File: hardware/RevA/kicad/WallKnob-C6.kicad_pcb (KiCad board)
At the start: 2 copper layers, 58 x 58 mm, 10 parts, among them SW1 EC11+PUSH, U1 ESP32-C6-MINI-1

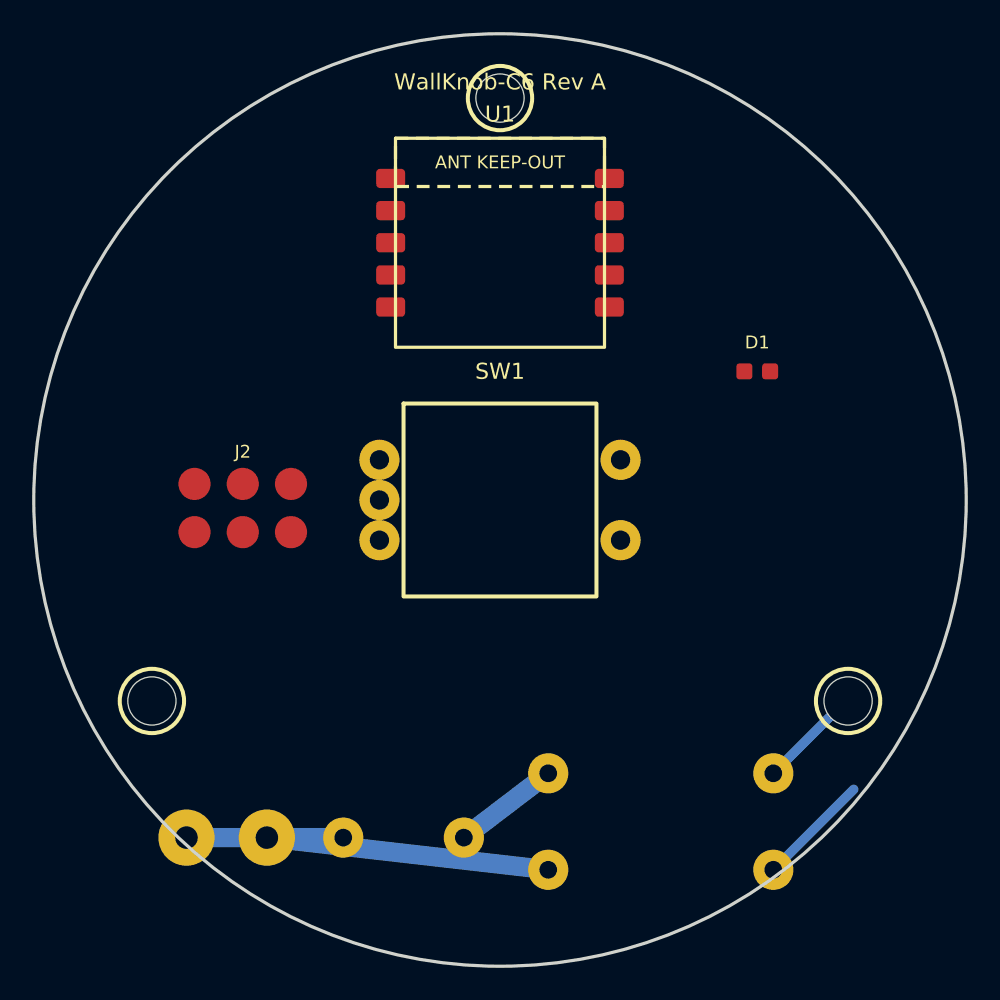
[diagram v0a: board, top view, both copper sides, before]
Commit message: Fix Rev A component placement inside PCB outline
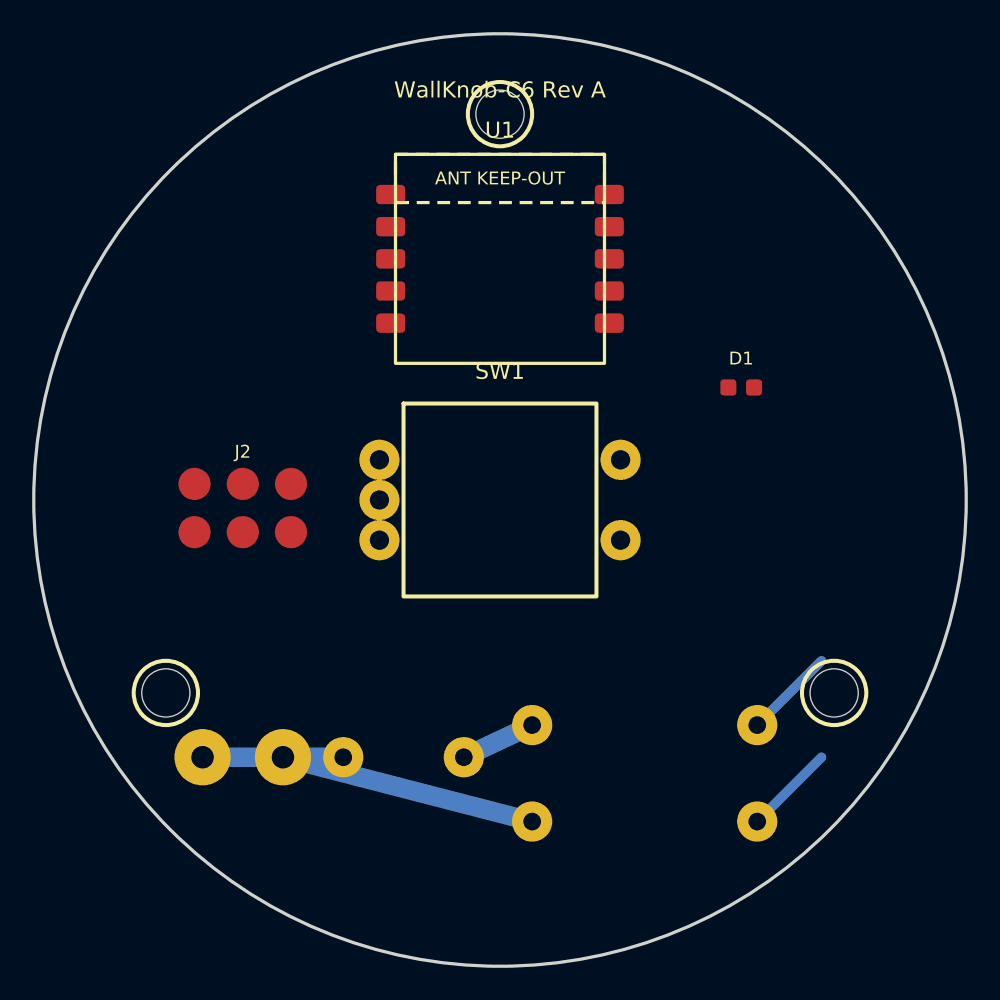
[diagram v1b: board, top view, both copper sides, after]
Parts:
- moved J1 5.10 mm to (84.0, 116.0)
- moved F1 5.00 mm to (94.0, 116.0)
- moved PS1 3.16 mm to (109.0, 117.0)
- moved D1 1.41 mm to (115.0, 93.0)
- moved H2 1.00 mm to (79.2, 112.0)
- moved H3 1.00 mm to (120.8, 112.0)
- moved H1 1.00 mm to (100.0, 76.0)
- moved U1 1.00 mm to (100.0, 85.0)
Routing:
- net L_FUSED: track 6.60 -> 4.70 mm
- net N_IN: track 17.6 -> 16.0 mm
- net GND: track 7.07 -> 5.66 mm
- net L_IN: track 9.75 -> 8.75 mm
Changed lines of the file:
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@@
   (net 13 "UART_RX")
   (gr_circle (center 100 100) (end 129 100) (stroke (width 0.2) (type solid)) (fill none) (layer "Edge.Cuts"))
-  (gr_line (start 82 112) (end 118 112) (stroke (width 0.3) (type solid)) (layer "B.SilkS"))
-  (gr_text "PRIMARY" (at 100 119) (layer "B.SilkS") (effects (font (size 1 1) (thickness 0.18)) (justify mirror)))
+  (gr_line (start 78 111) (end 122 111) (stroke (width 0.3) (type solid)) (layer "B.SilkS"))
+  (gr_text "PRIMARY" (at 100 117) (layer "B.SilkS") (effects (font (size 1 1) (thickness 0.18)) (justify mirror)))
   (gr_text "SELV" (at 100 106) (layer "B.SilkS") (effects (font (size 1 1) (thickness 0.18)) (justify mirror)))
-  (gr_text "WallKnob-C6 Rev A" (at 100 74) (layer "F.SilkS") (effects (font (size 1 1) (thickness 0.18))))
-  (footprint "MountingHole_1" (layer "F.Cu") (at 100.000 75.000)
+  (gr_text "WallKnob-C6 Rev A" (at 100 74.5) (layer "F.SilkS") (effects (font (size 1 1) (thickness 0.18))))
+  (footprint "MountingHole_1" (layer "F.Cu") (at 100.000 76.000)
     (property "Reference" "H1" (at 0 -3 0) (layer "F.SilkS") hide (effects (font (size 1 1) (thickness 0.15))))
     (fp_circle (center 0 0) (end 2 0) (stroke (width 0.25) (type solid)) (fill none) (layer "F.SilkS"))
     (pad "" np_thru_hole circle (at 0 0) (size 3.0 3.0) (drill 3.0) (layers "*.Cu" "*.Mask"))
   )
-  (footprint "MountingHole_2" (layer "F.Cu") (at 78.349 112.500)
+  (footprint "MountingHole_2" (layer "F.Cu") (at 79.216 112.000)
     (property "Reference" "H2" (at 0 -3 0) (layer "F.SilkS") hide (effects (font (size 1 1) (thickness 0.15))))
     (fp_circle (center 0 0) (end 2 0) (stroke (width 0.25) (type solid)) (fill none) (layer "F.SilkS"))
     (pad "" np_thru_hole circle (at 0 0) (size 3.0 3.0) (drill 3.0) (layers "*.Cu" "*.Mask"))
   )
-  (footprint "MountingHole_3" (layer "F.Cu") (at 121.651 112.500)
+  (footprint "MountingHole_3" (layer "F.Cu") (at 120.784 112.000)
     (property "Reference" "H3" (at 0 -3 0) (layer "F.SilkS") hide (effects (font (size 1 1) (thickness 0.15))))
     (fp_circle (center 0 0) (end 2 0) (stroke (width 0.25) (type solid)) (fill none) (layer "F.SilkS"))
@@
     (pad "S2" thru_hole circle (at 7.5 2.5) (size 2.5 2.5) (drill 1.2) (layers *.Cu *.Mask) (net 5 "GND"))
   )
-  (footprint "ESP32-C6-MINI-1_CUSTOM" (layer "F.Cu") (at 100 84)
+  (footprint "ESP32-C6-MINI-1_CUSTOM" (layer "F.Cu") (at 100 85)
     (property "Reference" "U1" (at 0 -8 0) (layer "F.SilkS") (effects (font (size 1 1) (thickness 0.15))))
     (property "Value" "ESP32-C6-MINI-1" (at 0 8 0) (layer "F.Fab") hide (effects (font (size 1 1) (thickness 0.15))))
@@
     (pad "10" smd roundrect (at -6.8 -4) (size 1.8 1.2) (layers "F.Cu" "F.Paste" "F.Mask") (roundrect_rratio 0.2) (net 13 "UART_RX"))
   )
-  (footprint "LED_0603" (layer "F.Cu") (at 116 92)
+  (footprint "LED_0603" (layer "F.Cu") (at 115 93)
     (property "Reference" "D1" (at 0 -1.8 0) (layer "F.SilkS") (effects (font (size 0.8 0.8) (thickness 0.12))))
     (pad "1" smd roundrect (at -0.8 0) (size 1 1) (layers "F.Cu" "F.Paste" "F.Mask") (roundrect_rratio 0.2) (net 9 "LED"))
     (pad "2" smd roundrect (at 0.8 0) (size 1 1) (layers "F.Cu" "F.Paste" "F.Mask") (roundrect_rratio 0.2) (net 5 "GND"))
   )
-  (footprint "AC_IN_2P_CUSTOM" (layer "B.Cu") (at 83 121)
+  (footprint "AC_IN_2P_CUSTOM" (layer "B.Cu") (at 84 116)
     (property "Reference" "J1" (at 0 4 0) (layer "B.SilkS") (effects (font (size 1 1) (thickness 0.15)) (justify mirror)))
     (fp_rect (start -5 -3) (end 5 3) (stroke (width 0.25) (type solid)) (fill none) (layer "B.SilkS"))
@@
     (pad "2" thru_hole circle (at 2.5 0) (size 3.5 3.5) (drill 1.4) (layers *.Cu *.Mask) (net 2 "N_IN"))
   )
-  (footprint "FUSE_THT_CUSTOM" (layer "B.Cu") (at 94 121)
+  (footprint "FUSE_THT_CUSTOM" (layer "B.Cu") (at 94 116)
     (property "Reference" "F1" (at 0 3 0) (layer "B.SilkS") (effects (font (size 1 1) (thickness 0.15)) (justify mirror)))
     (pad "1" thru_hole circle (at -3.75 0) (size 2.5 2.5) (drill 1.1) (layers *.Cu *.Mask) (net 1 "L_IN"))
     (pad "2" thru_hole circle (at 3.75 0) (size 2.5 2.5) (drill 1.1) (layers *.Cu *.Mask) (net 3 "L_FUSED"))
   )
-  (footprint "IRM-01-3.3_CUSTOM_VERIFY" (layer "B.Cu") (at 110 120)
+  (footprint "IRM-01-3.3_CUSTOM_VERIFY" (layer "B.Cu") (at 109 117)
     (property "Reference" "PS1" (at 0 6 0) (layer "B.SilkS") (effects (font (size 1 1) (thickness 0.15)) (justify mirror)))
     (property "Value" "IRM-01-3.3 VERIFY FOOTPRINT" (at 0 -6 0) (layer "B.Fab") hide (effects (font (size 1 1) (thickness 0.15)) (justify mirror)))
@@
     (pad "6" smd circle (at 3 1) (size 2 2) (layers "F.Cu" "F.Mask") (net 10 "BOOT"))
   )
-  (segment (start 80.5 121) (end 90.25 121) (width 1.2) (layer "B.Cu") (net 1))
-  (segment (start 97.75 121) (end 103 117) (width 1.2) (layer "B.Cu") (net 3))
-  (segment (start 85.5 121) (end 103 123) (width 1.2) (layer "B.Cu") (net 2))
-  (segment (start 117 117) (end 121 113) (width 0.6) (layer "B.Cu") (net 4))
-  (segment (start 117 123) (end 122 118) (width 0.6) (layer "B.Cu") (net 5))
-  (gr_rect (start 80 110.5) (end 122 113.5) (stroke (width 0.2) (type dash)) (fill none) (layer "B.SilkS"))
+  (segment (start 81.5 116) (end 90.25 116) (width 1.2) (layer "B.Cu") (net 1))
+  (segment (start 97.75 116) (end 102 114) (width 1.2) (layer "B.Cu") (net 3))
+  (segment (start 86.5 116) (end 102 120) (width 1.2) (layer "B.Cu") (net 2))
+  (segment (start 116 114) (end 120 110) (width 0.6) (layer "B.Cu") (net 4))
+  (segment (start 116 120) (end 120 116) (width 0.6) (layer "B.Cu") (net 5))
+  (gr_rect (start 79 109.5) (end 121 112.5) (stroke (width 0.2) (type dash)) (fill none) (layer "B.SilkS"))
 )
